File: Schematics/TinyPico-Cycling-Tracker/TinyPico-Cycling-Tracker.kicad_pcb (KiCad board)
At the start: 2 copper layers, 105.2 x 70.1 mm, 17 parts, among them J1 Conn_01x05, J4 Conn_01x05_Socket, SW2 SW_Push, U10 MicroSD Card Adapter, U6 module_mpu6050, U7 SSD1306 0.96" OLED, U8 TinyPico, U9 GPS6MV2

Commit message: chore: add two pin SPST button
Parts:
- SW2: footprint Button_Switch_THT:SW_TH_Tactile_Omron_B3F-102x -> SPST_Button:SPST_Button
- moved U7 25.1 mm to (138.4, 65.4), turned to 180 degrees
- moved R2 24.2 mm to (152.4, 74.3)
- moved U6 23.6 mm to (121.2, 74.3), turned to -90 degrees
- moved SW2 20.6 mm to (148.6, 82.5)
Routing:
- net GND1: track 98.6 -> 41.7 mm
- net /Upper Board/SW_S: track 64.0 -> 18.7 mm, vias 2 -> 0
- net VCC1: track 72.4 -> 39.9 mm, vias 2 -> 1
- net /Upper Board/SDA: track 68.9 -> 52.5 mm, vias 4 -> 2
- net /Upper Board/SCL: track 68.8 -> 59.6 mm, vias 4 -> 2

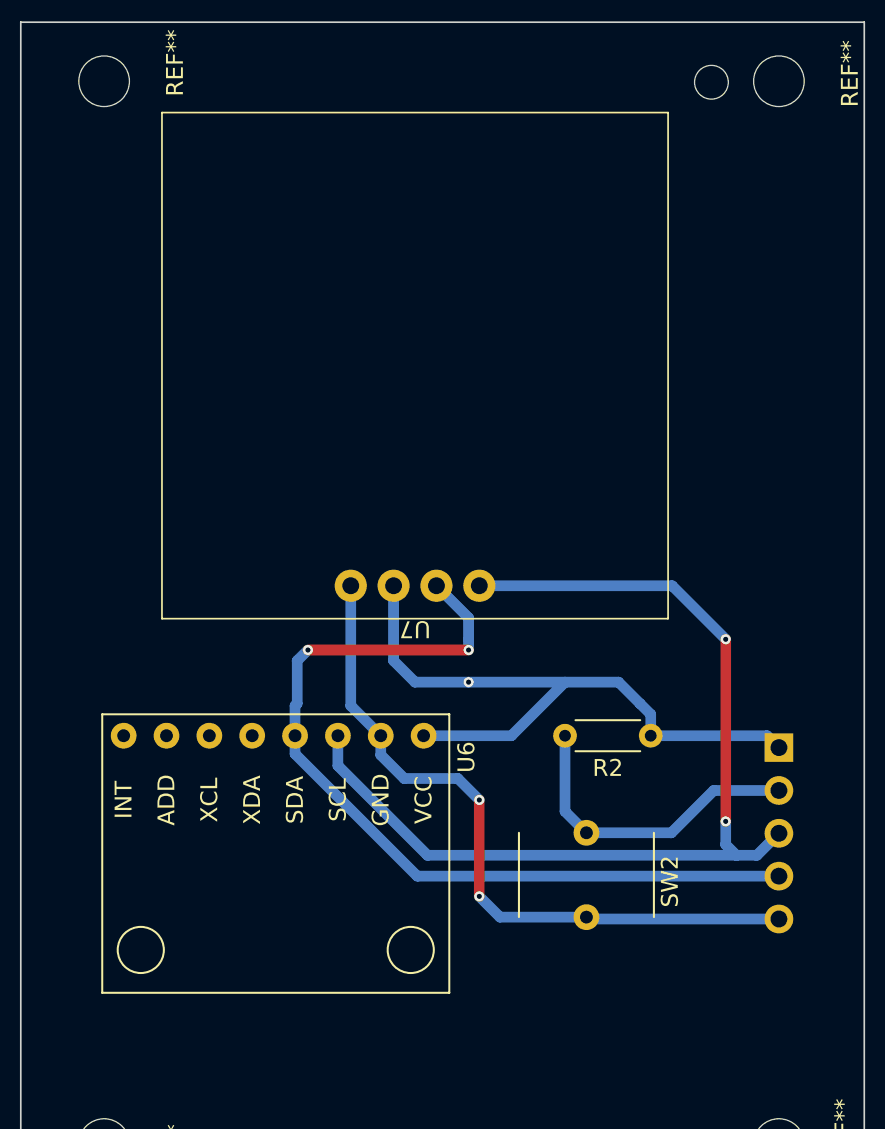
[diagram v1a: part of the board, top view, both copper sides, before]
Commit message: chore: move upper board pcb
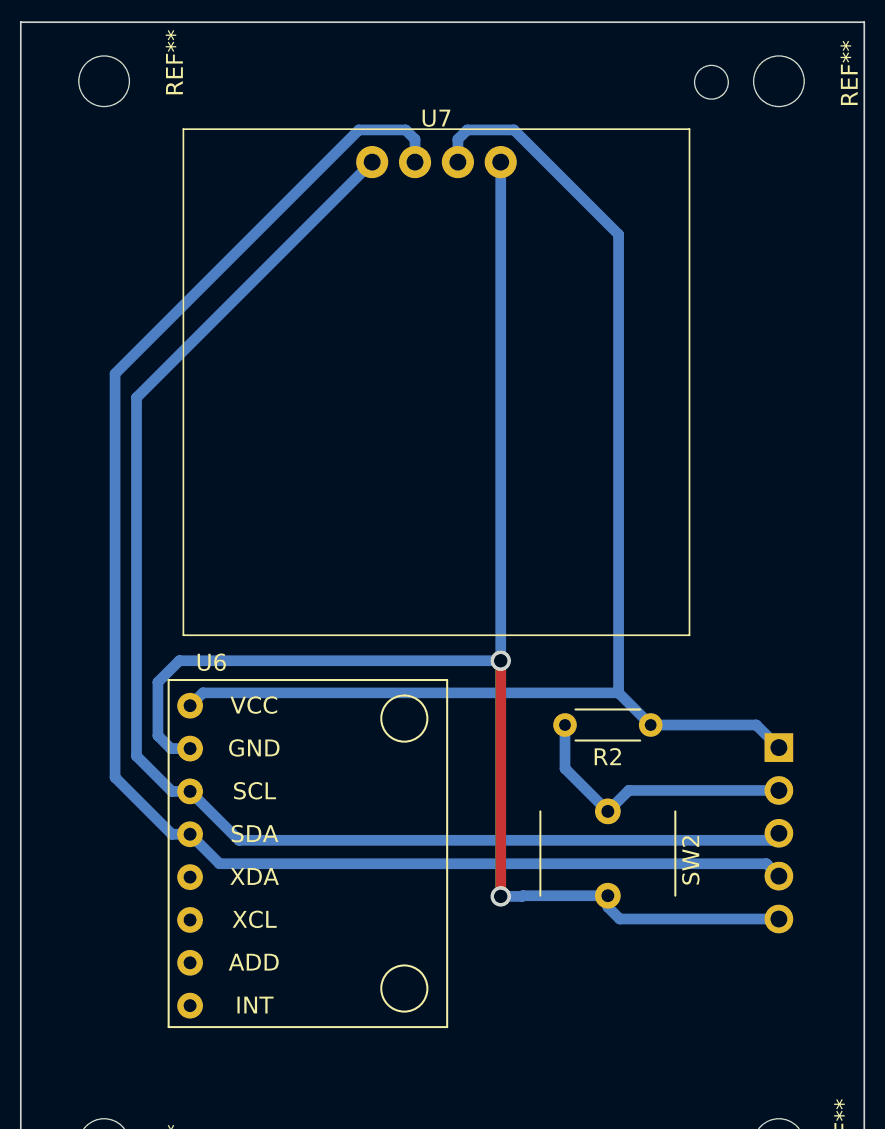
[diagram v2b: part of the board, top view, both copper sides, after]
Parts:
- moved U7 25.1 mm to (139.7, 40.3), turned to 0 degrees
- moved U6 16.5 mm to (125.1, 90.3), turned to 0 degrees
- moved SW2 1.80 mm to (149.9, 81.3)
- moved R2 0.64 mm to (152.4, 73.7)
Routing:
- net GND1: track 41.7 -> 87.2 mm
- net /Upper Board/SDA: track 52.5 -> 91.1 mm, vias 2 -> 0
- net VCC1: track 39.9 -> 77.4 mm, vias 1 -> 0
- net /Upper Board/SCL: track 59.6 -> 81.3 mm, vias 2 -> 0
- net /Upper Board/SW_S: track 18.7 -> 16.8 mm

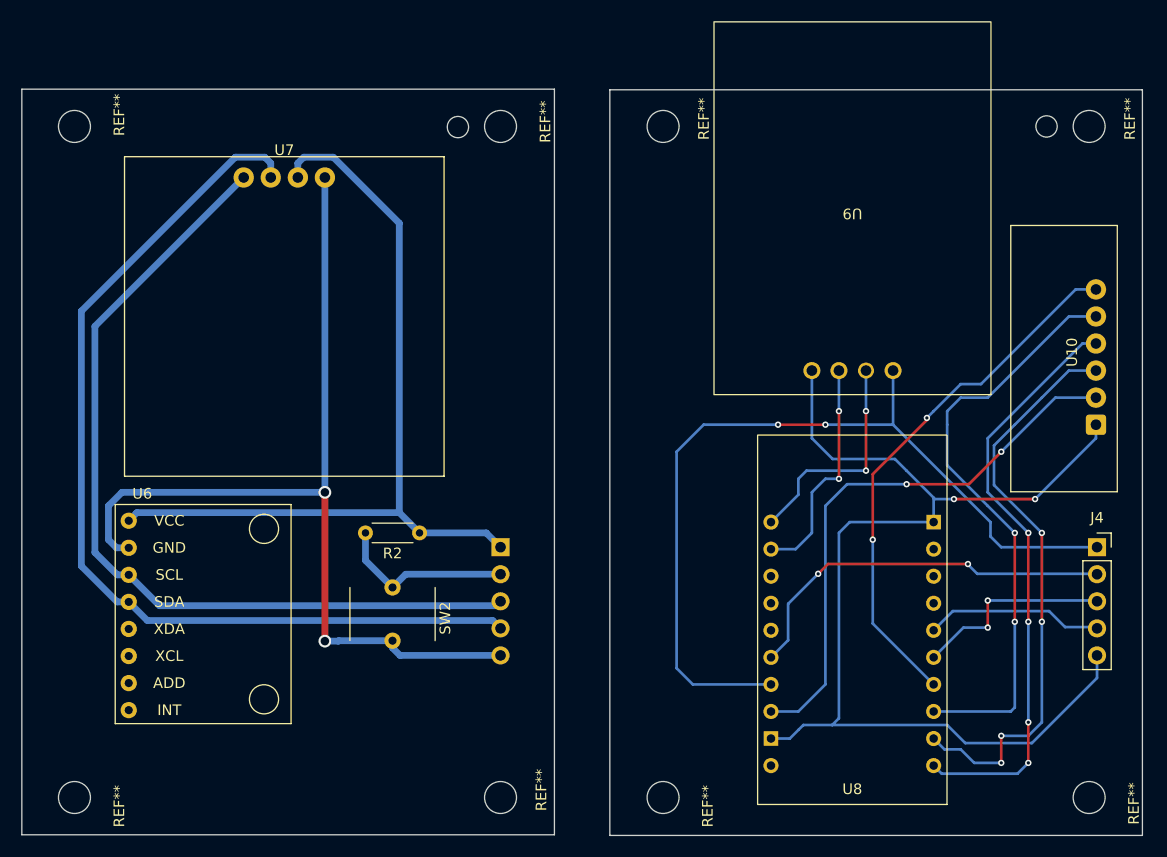
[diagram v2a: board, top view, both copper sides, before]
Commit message: fix: down PCB to use less vias
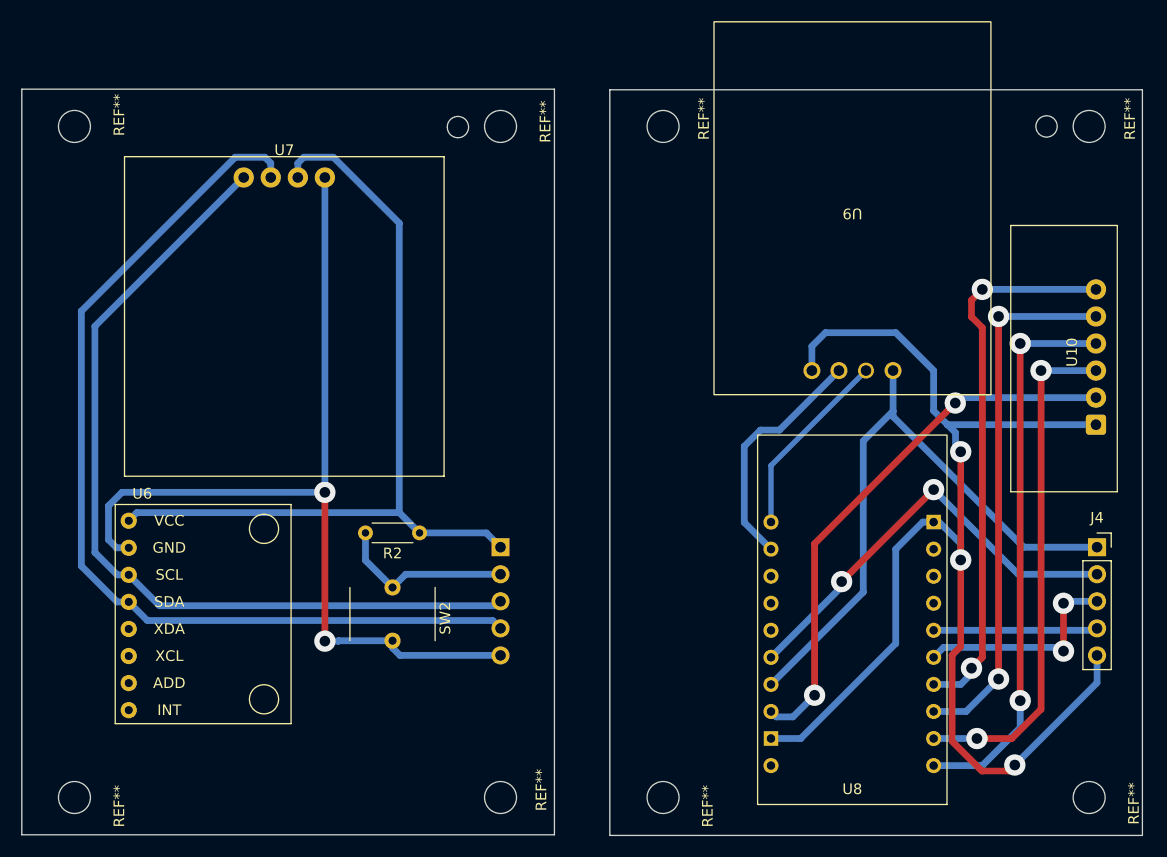
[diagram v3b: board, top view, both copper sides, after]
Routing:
- net VCC2: track 80.9 -> 58.9 mm, vias 2 -> 0
- net GND2: track 105.6 -> 120.8 mm, vias 2 -> 3
- net Net-(U10-MISO): track 54.5 -> 48.2 mm, vias 4 -> 2
- net Net-(U10-SCK): track 55.9 -> 50.5 mm
- net /Bottom Board/SW_TP: track 36.6 -> 40.7 mm
- net Net-(U8-IO25): track 21.2 -> 17.9 mm, vias 2 -> 0
- net Net-(U10-MOSI): track 55.5 -> 52.8 mm, vias 4 -> 2
- net Net-(U10-VCC): track 52.5 -> 50.7 mm
- net Net-(U10-CS): track 50.4 -> 52.0 mm
- net /Bottom Board/SCL: track 18.9 -> 20.4 mm
- net /Bottom Board/SDA: track 16.6 -> 15.4 mm
- net Net-(U8-IO26): track 21.5 -> 22.5 mm, vias 2 -> 0

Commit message: chore: position of Push Button & Mounting Holes
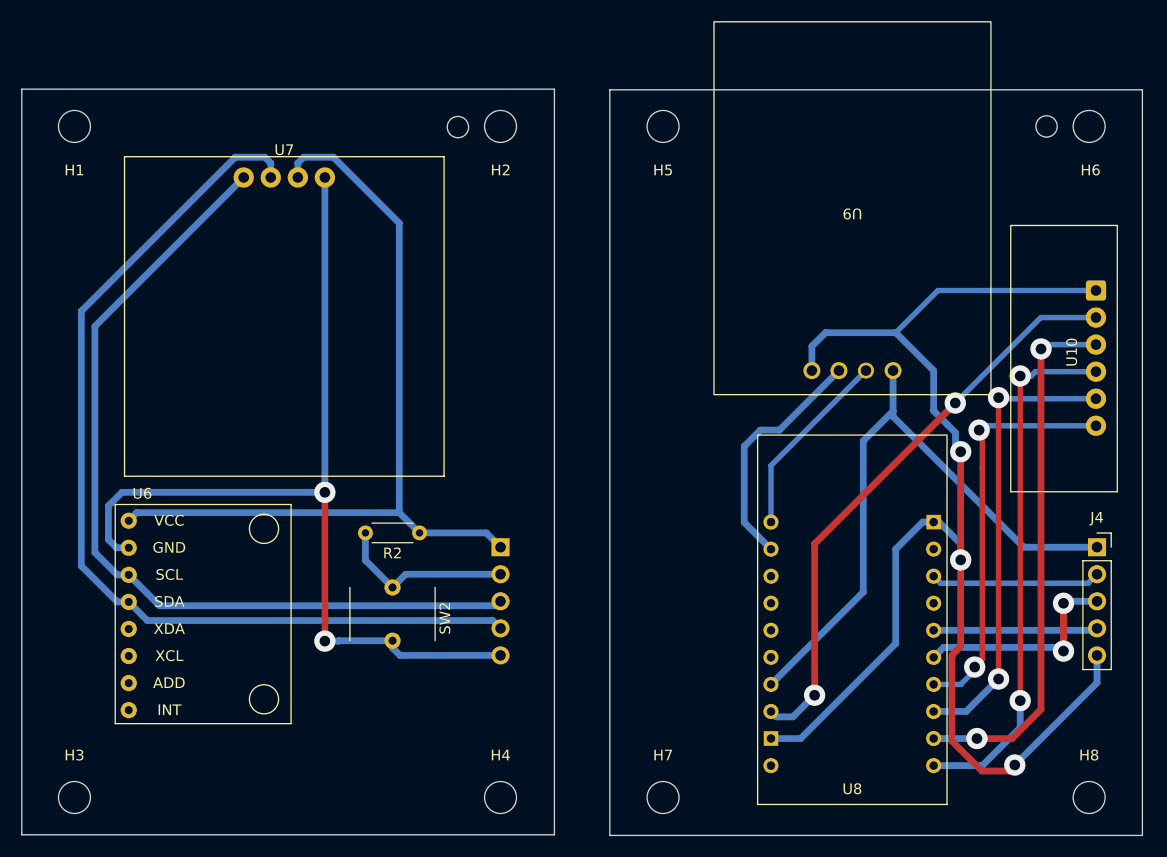
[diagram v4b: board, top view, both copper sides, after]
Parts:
- removed REF** (x8): MountingHole_3mm, MountingHole:MountingHole_3mm
- added H1: MountingHole, MountingHole:MountingHole_3mm, F.Cu at (120.0, 35.5)
- added H2: MountingHole, MountingHole:MountingHole_3mm, F.Cu at (160.0, 35.5)
- added H3: MountingHole, MountingHole:MountingHole_3mm, F.Cu at (120.0, 98.5)
- added H4: MountingHole, MountingHole:MountingHole_3mm, F.Cu at (160.0, 98.5)
- added H5: MountingHole, MountingHole:MountingHole_3mm, F.Cu at (175.3, 35.5)
- added H6: MountingHole, MountingHole:MountingHole_3mm, F.Cu at (215.3, 35.5)
- added H7: MountingHole, MountingHole:MountingHole_3mm, F.Cu at (175.3, 98.5)
- added H8: MountingHole, MountingHole:MountingHole_3mm, F.Cu at (215.3, 98.5)
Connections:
- U8 pad 16: /Bottom Board/SW_TP -> unconnected-(U8-IO4-Pad16)
- U8 pad 8: unconnected-(U8-IO33-Pad8) -> /Bottom Board/SW_TP
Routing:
- net /Bottom Board/SW_TP: track 40.7 -> 16.0 mm, vias 2 -> 0
- net Net-(U10-CS): track 52.0 -> 38.8 mm
- net Net-(U10-SCK): track 50.5 -> 43.0 mm
- net GND2: track 120.8 -> 127.3 mm
- net Net-(U10-VCC): track 50.7 -> 54.6 mm
- net Net-(U10-MOSI): track 52.8 -> 49.9 mm
- net Net-(U10-MISO): track 48.2 -> 50.4 mm

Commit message: chore: INT in schematic and PCB
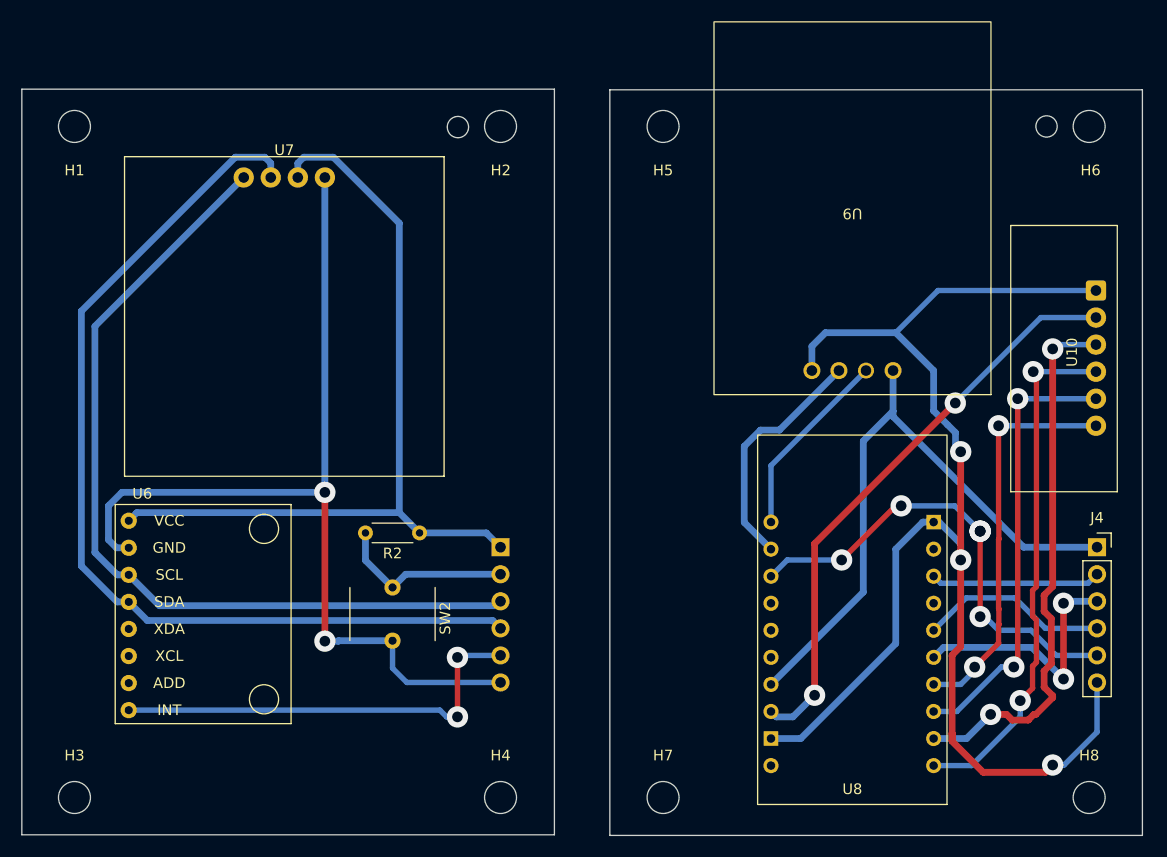
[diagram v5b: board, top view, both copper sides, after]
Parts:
- J1: value Conn_01x05 -> Conn_01x06; footprint Connector_PinHeader_2.54mm:PinHeader_1x05_P2.54mm_Vertical -> Connector_PinHeader_2.54mm:PinHeader_1x06_P2.54mm_Vertical
- J4: value Conn_01x05_Socket -> Conn_01x06_Socket; footprint Connector_PinSocket_2.54mm:PinSocket_1x05_P2.54mm_Vertical -> Connector_PinSocket_2.54mm:PinSocket_1x06_P2.54mm_Vertical
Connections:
- J1 pad 5: GND1 -> /Upper Board/INT
- J4 pad 5: GND2 -> /Bottom Board/INT
- U6 pad 8: unconnected-(U6-INT-Pad8) -> /Upper Board/INT
- U8 pad 13: unconnected-(U8-IO27-Pad13) -> /Bottom Board/INT
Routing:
- net /Bottom Board/INT: track 0.00 -> 45.0 mm, vias 0 -> 5
- net /Upper Board/INT: track 0.00 -> 40.8 mm, vias 0 -> 2
- net /Bottom Board/SCL: track 20.4 -> 24.1 mm
- net /Bottom Board/SDA: track 15.4 -> 18.0 mm
- net GND1: track 87.2 -> 89.4 mm
- net GND2: track 127.3 -> 128.6 mm
- net Net-(U10-MISO): track 50.4 -> 51.4 mm
- net Net-(U10-CS): track 38.8 -> 37.7 mm
- net Net-(U10-SCK): track 43.0 -> 42.0 mm
- net Net-(U10-MOSI): track 49.9 -> 49.4 mm
